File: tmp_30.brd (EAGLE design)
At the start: 31.8 x 81.7 mm, 0 parts

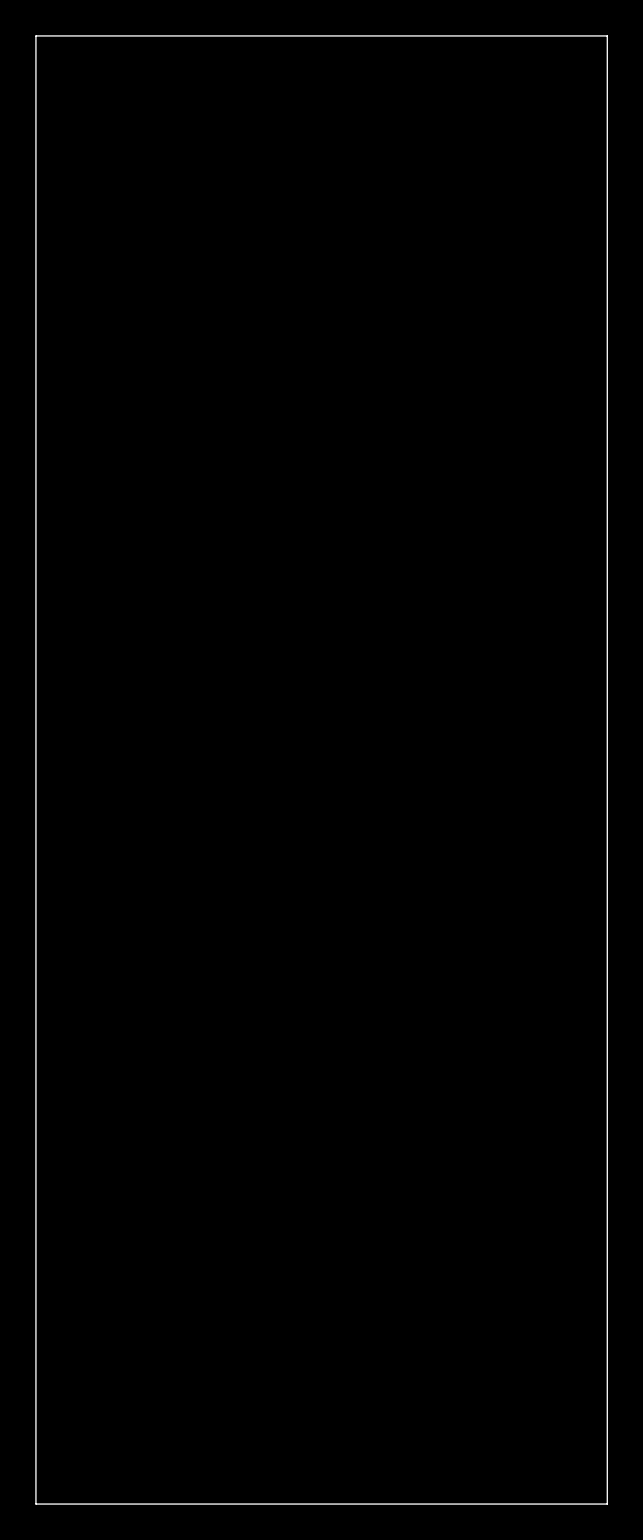
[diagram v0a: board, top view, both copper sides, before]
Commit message: modified display
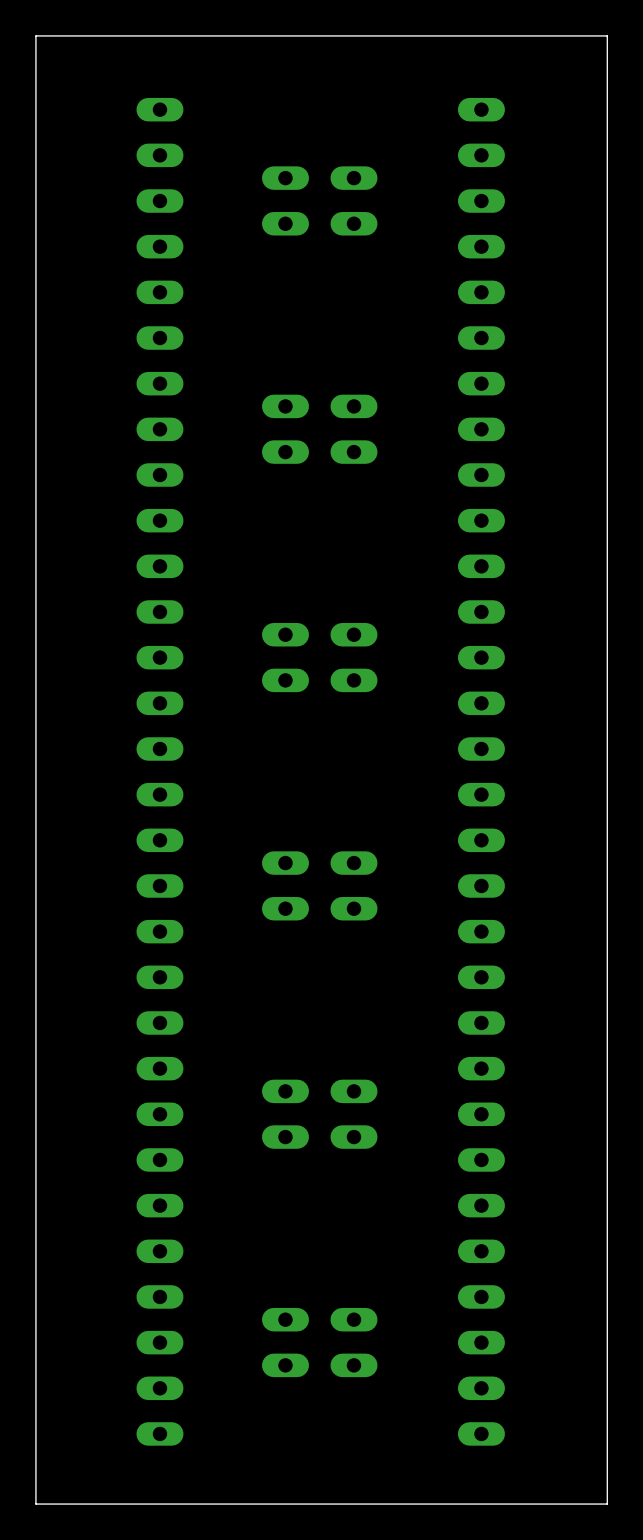
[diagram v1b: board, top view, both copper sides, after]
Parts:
- added LL0, LL1, LL10, LL11, LL12, LL13, LL14, LL15, LL16, LL17, LL18, LL19, LL2, LL20, LL21, LL22, LL23, LL24, LL25, LL26, LL27, LL28, LL29, LL3, LL4, LL5, LL6, LL7, LL8, LL9, LS0, LS1, LS10, LS11, LS2, LS3, LS4, LS5, LS6, LS7, LS8, LS9, RL0, RL1, RL10, RL11, RL12, RL13, RL14, RL15, RL16, RL17, RL18, RL19, RL2, RL20, RL21, RL22, RL23, RL24, RL25, RL26, RL27, RL28, RL29, RL3, RL4, RL5, RL6, RL7, RL8, RL9, RS0, RS1, RS10, RS11, RS2, RS3, RS4, RS5, RS6, RS7, RS8, RS9: (no value), SparkFun-Connectors:1X01_OVAL_PIN_AUTO
